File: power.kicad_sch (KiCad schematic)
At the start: 41 parts, among them J10 Conn_01x02, J11 Solar_Cell, J9 Battery_Cell, Q1 AO4882, Q3 AO4882, U2 BQ25798, U5 TPS6282x

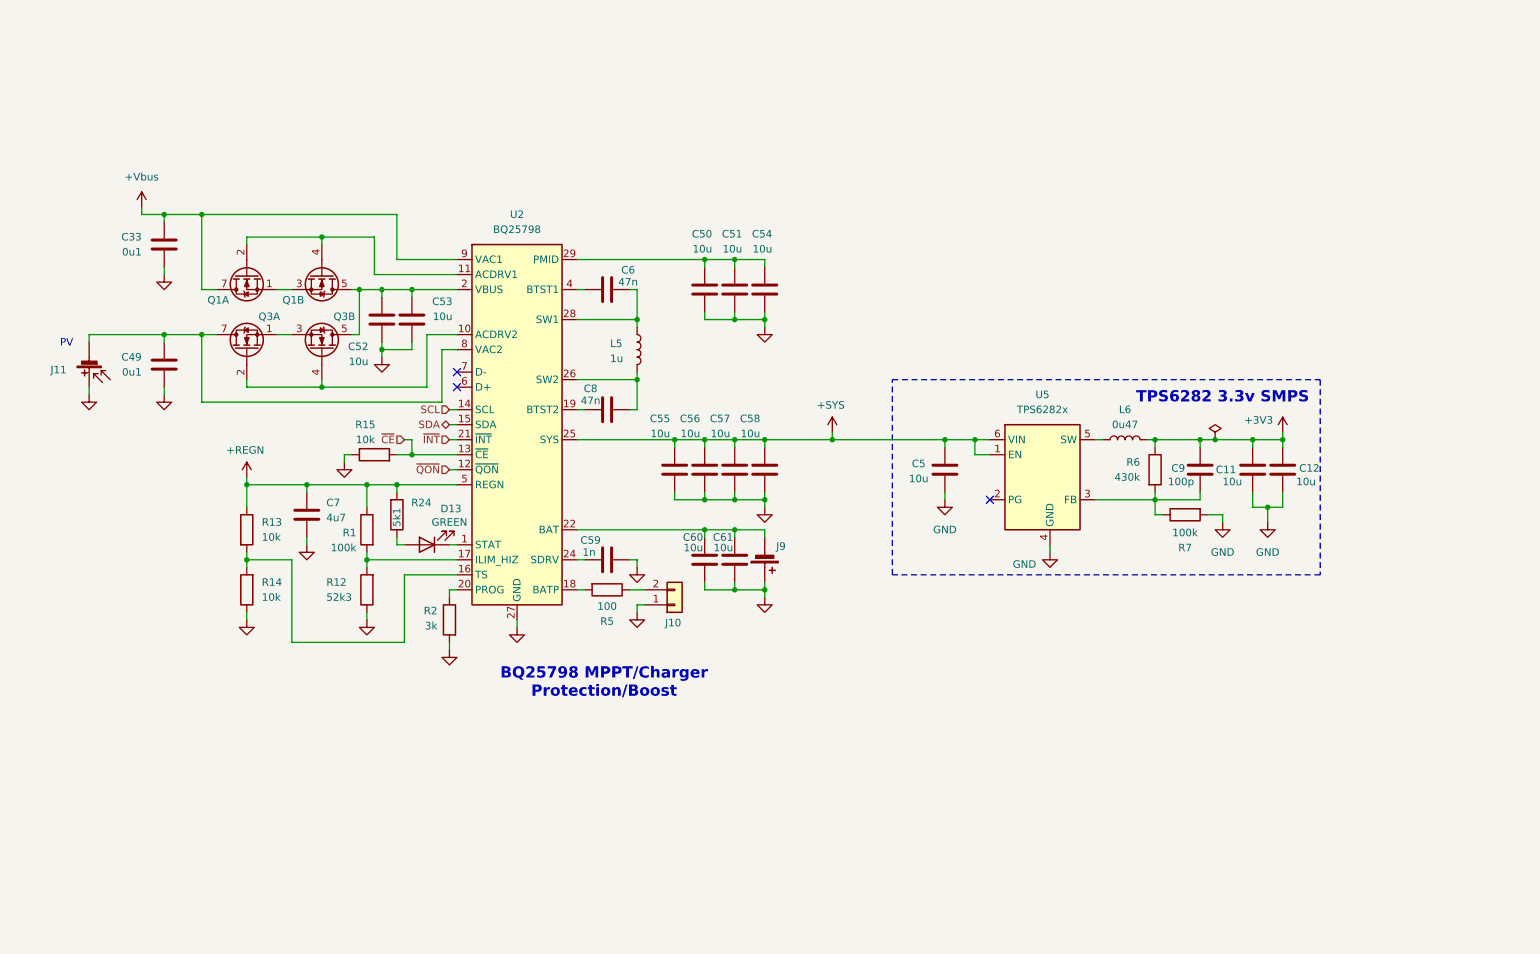
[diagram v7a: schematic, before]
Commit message: schem: add usbc pwer connector
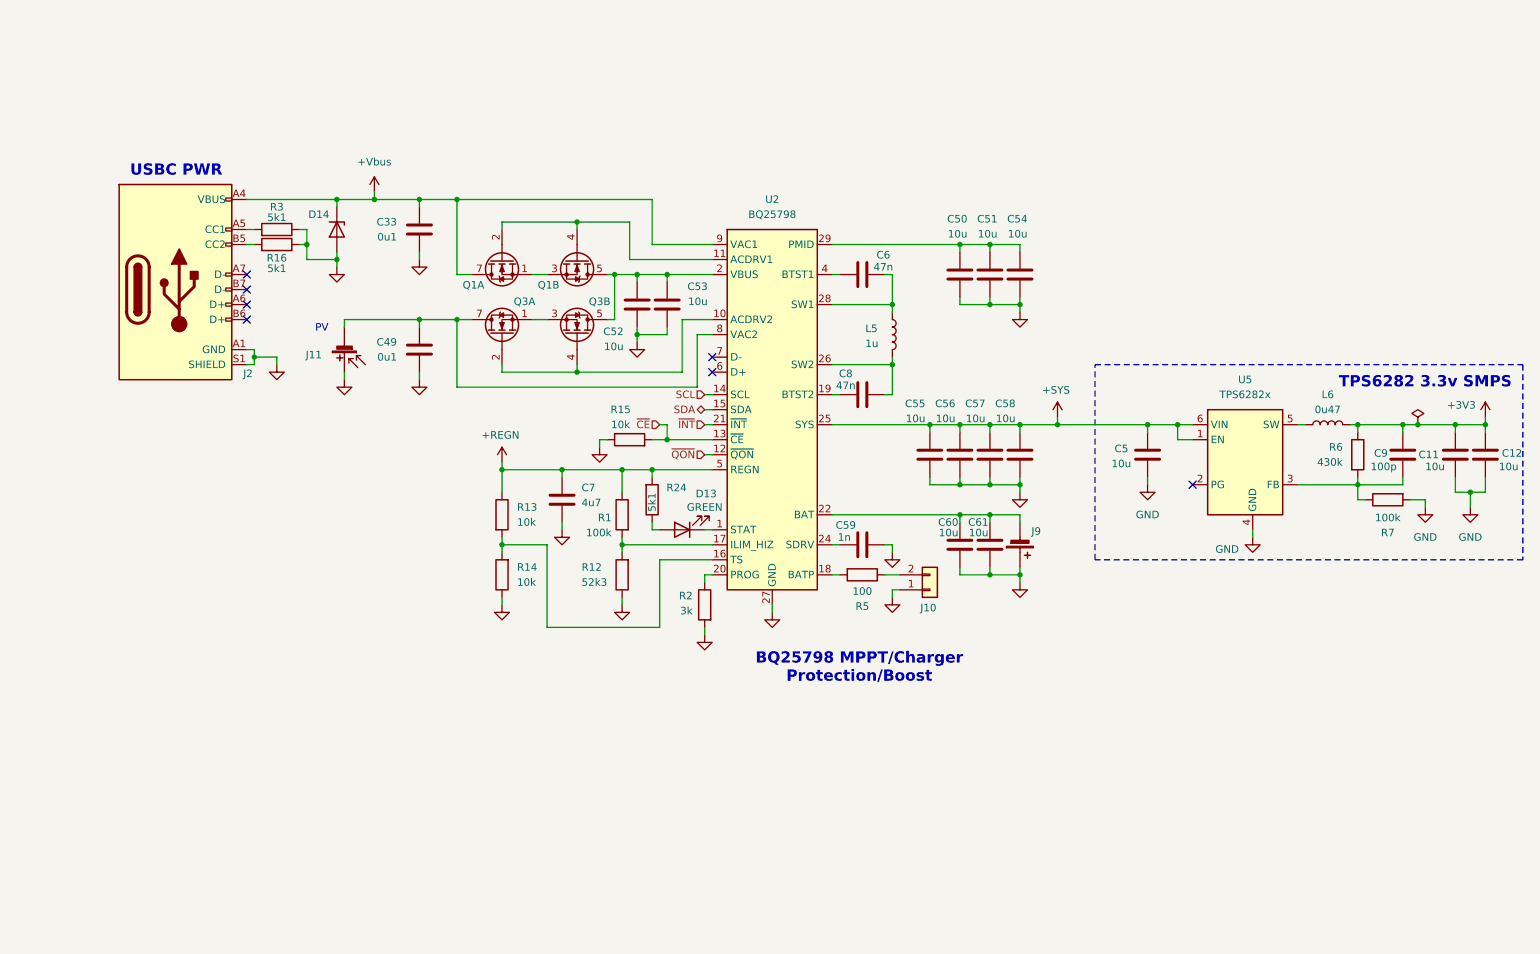
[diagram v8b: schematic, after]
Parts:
- added D14: H5VU10U, GLCS:Diode_DFN1006, symbol GLCS:H5VU10U
- added J2: USB_C_Receptacle_USB2.0_14P, Connector_USB:USB_C_Receptacle_HRO_TYPE-C-31-M-12, symbol Connector:USB_C_Receptacle_USB2.0_14P
- added R16, R3: 5k1, Resistor_SMD:R_0402_1005Metric, symbol Device:R
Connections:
- net +Vbus: now also D14.1 (K), J2.A4 (VBUS), J2.A9 (VBUS), J2.B4 (VBUS), J2.B9 (VBUS)
- net GND: now also D14.2 (A), J2.A1 (GND), J2.A12 (GND), J2.B1 (GND), J2.B12 (GND), J2.S1 (SHIELD), R16.1, R3.1
- new net: J2.A5 (CC1), R3.2
- new net: J2.B5 (CC2), R16.2
- no-connect marks 3 -> 7
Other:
- note added: "USBC PWR"
- moved on the sheet: C11, C12, C33, C49, C5, C50, C51, C52, C53, C54, C55, C56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
